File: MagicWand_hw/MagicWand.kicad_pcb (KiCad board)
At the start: 4 copper layers, 103 x 14.4 mm, 90 parts, among them M1 MOTOR_NO_CONTACTS, Q1 M28S, Q2 M28S, Q3 M28S, Q4 M28S, Q5 IRLML6401, Q6 M28S, Q7 IRLML6401, SW1 BUTTON, SW2 BUTTON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

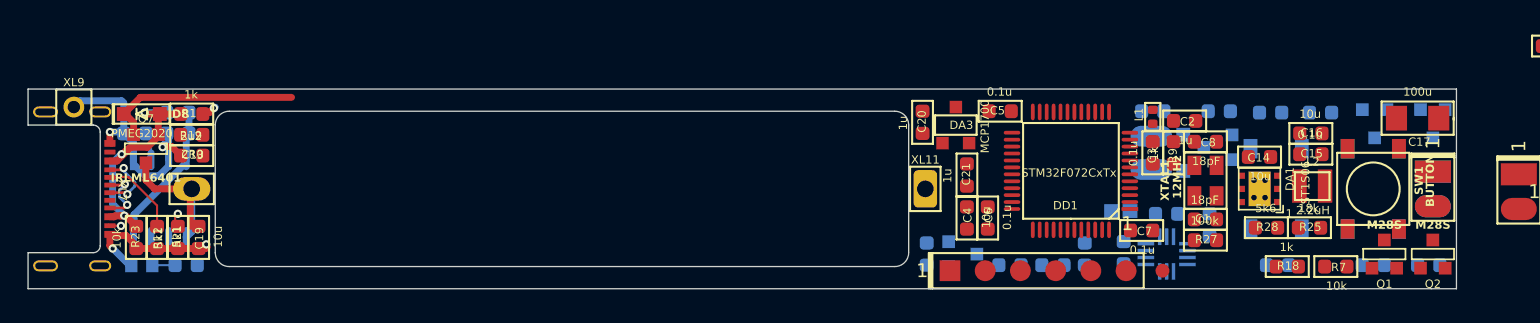
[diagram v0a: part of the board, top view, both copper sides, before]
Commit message: Remove quartz, PCB length decreased to 99mm
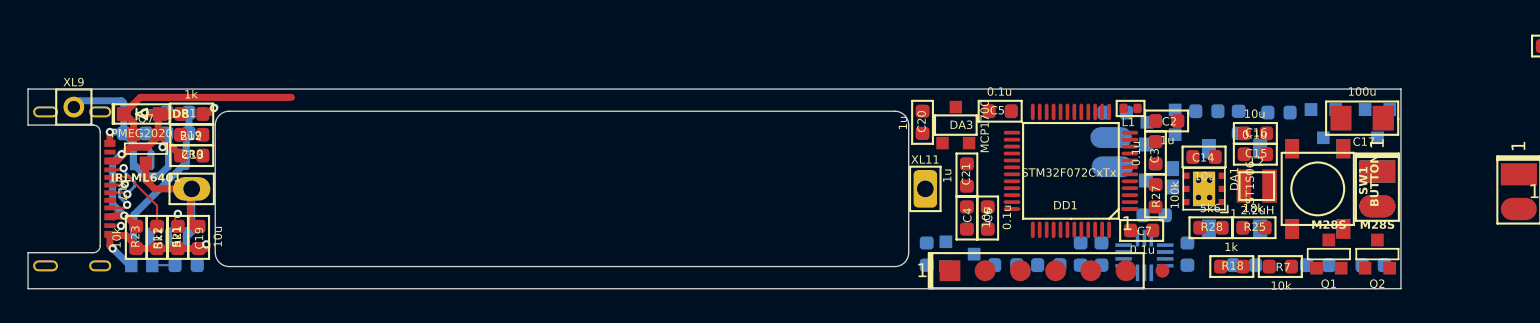
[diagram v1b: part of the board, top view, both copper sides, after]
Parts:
- removed C1, C8: 18pF, Capacitors:CAP_0603_Silks
- removed R9: 1k, Resistors:RES_0603_Silks
- removed XTAL1: 12MHz, Quartz:03225C4
- moved R27 4.82 mm to (185.3, 102.7), turned to 90 degrees
- moved Q6 4.48 mm to (185.7, 97.4)
- moved F1 4.41 mm to (186.5, 101.4), turned to -90 degrees
- moved C14 4.00 mm to (188.8, 99.9)
- moved C15 4.00 mm to (192.5, 99.7)
- moved C16 4.00 mm to (192.5, 98.2)
- moved C17 4.00 mm to (200.2, 97.1)
- moved DA1 4.00 mm to (188.8, 102.2)
- moved L2 4.00 mm to (192.6, 102.0)
- moved Q1 4.00 mm to (197.8, 106.9)
- moved Q2 4.00 mm to (201.3, 106.9)
- moved Q3 4.00 mm to (201.3, 97.5)
- moved R17 4.00 mm to (197.0, 107.7)
- moved R18 4.00 mm to (190.8, 107.8)
- moved R25 4.00 mm to (192.4, 105.0)
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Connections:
- DD1 pad 5: Net-(DD1-OSCIN) -> unconnected-(DD1-OSCIN-Pad5)
- DD1 pad 6: Net-(DD1-OSCOUT) -> unconnected-(DD1-OSCOUT-Pad6)
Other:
- board size 103 x 14.4 mm -> 99 x 14.4 mm

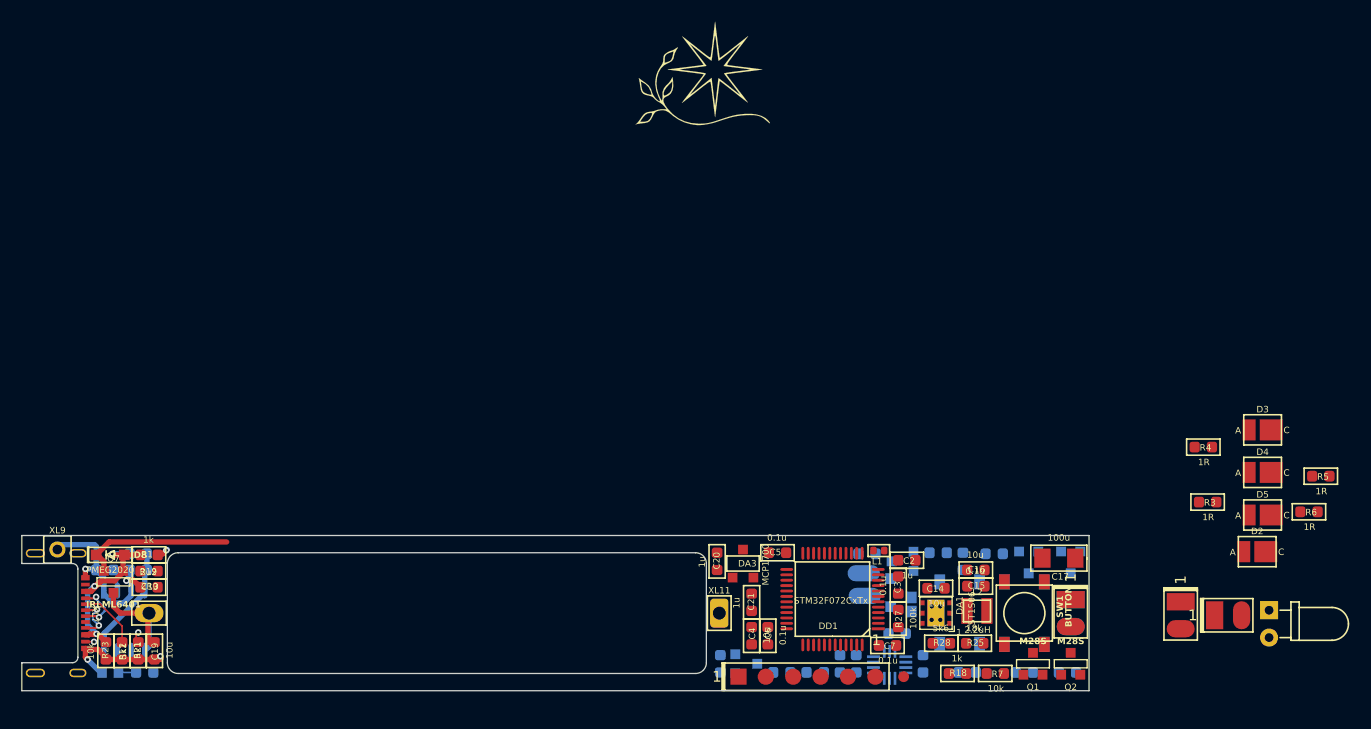
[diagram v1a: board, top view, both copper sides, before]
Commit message: USB conn changed to real one
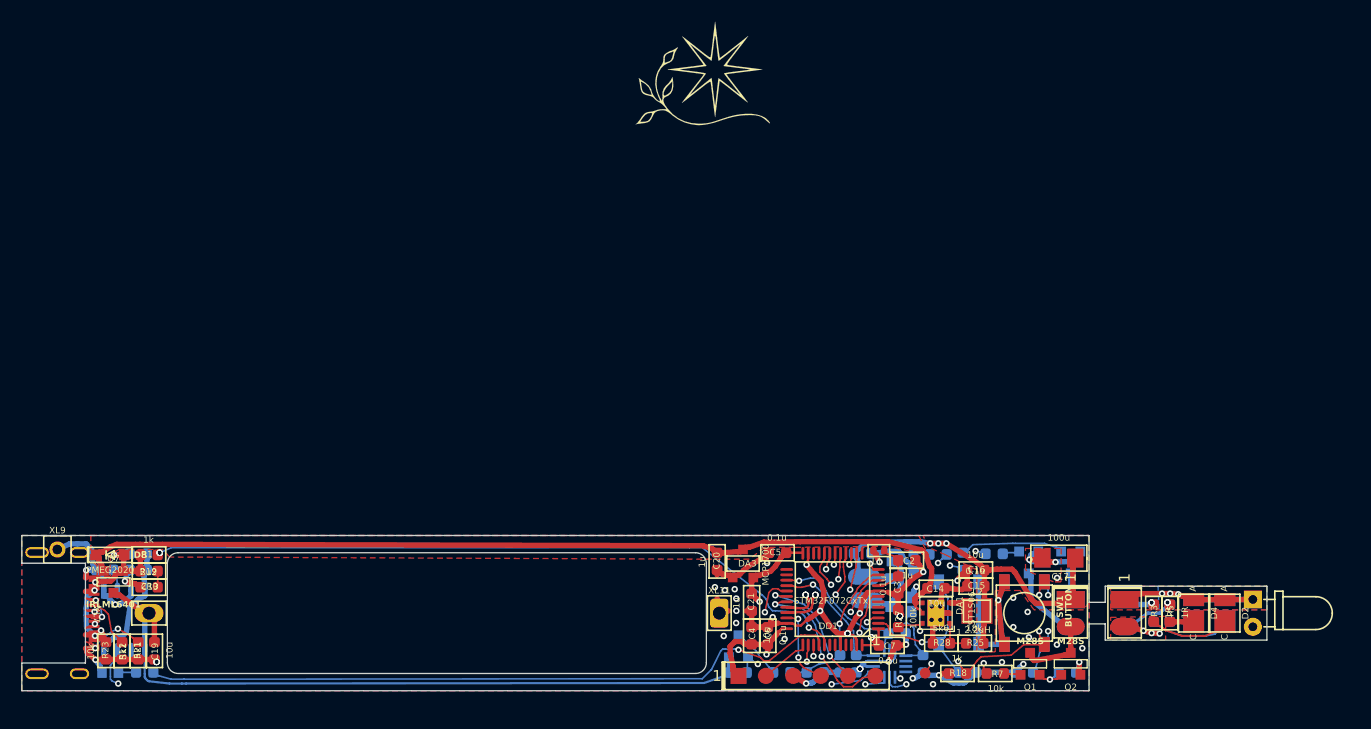
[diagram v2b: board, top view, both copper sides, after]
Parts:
- D3, D5, R4, R6, XL5: moved to B.Cu
- moved R5 18.9 mm to (210.5, 102.2), turned to 90 degrees
- moved D3 17.4 mm to (215.6, 102.2), turned to -90 degrees
- moved R4 16.1 mm to (209.0, 102.2), turned to 90 degrees
- moved R6 16.0 mm to (210.5, 102.2), turned to 90 degrees
- moved D4 14.5 mm to (212.7, 102.2), turned to -90 degrees
- moved R3 11.4 mm to (209.0, 102.2), turned to 90 degrees
- moved D5 11.1 mm to (212.7, 102.2), turned to -90 degrees
- moved XL5 9.60 mm to (206.3, 102.2), turned to -90 degrees
- moved D2 6.44 mm to (215.6, 102.2), turned to -90 degrees
- moved XL3 5.20 mm to (206.3, 102.2)
- moved TP1 2.02 mm to (187.8, 107.8)
- moved R14 1.84 mm to (170.4, 107.7), turned to 0 degrees
- moved D1 1.80 mm to (218.2, 102.2)
- moved Q5 1.78 mm to (170.5, 105.3), turned to 0 degrees
- moved XL8 0.44 mm to (182.4, 101.0)
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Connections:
- net /LED_PWR_EN renamed /PWR_EN
- net Net-(D1-PadA) renamed /LEDA
- net Net-(D1-PadC) renamed /LEDIRC
- net Net-(R3-Pad2) renamed /LEDGC
- net Net-(R5-Pad2) renamed /LEDWC
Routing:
- net GND: track 28.2 -> 260.4 mm, vias 4 -> 49
- net +PwrMCU: track 0.00 -> 83.4 mm, vias 0 -> 8
- net /USB_D+: track 4.14 -> 80.7 mm, vias 2 -> 5
- net /IS_CHARGING: track 0.00 -> 75.4 mm, vias 0 -> 2
- net /USB_D-: track 5.07 -> 80.1 mm, vias 2 -> 5
- net +PwrUnst: track 14.2 -> 88.1 mm
- net /SYS_LED: track 0.00 -> 65.2 mm, vias 0 -> 1
- net Net-(DD1-PB5): track 1.07 -> 66.2 mm, vias 1 -> 4
- net +BATT: track 11.2 -> 69.5 mm
- net +PwrCtrled: track 0.00 -> 40.6 mm, vias 0 -> 3
- net /BTN1: track 0.00 -> 31.9 mm, vias 0 -> 4
- net /BTN2: track 0.00 -> 27.0 mm, vias 0 -> 3
- net /ACC_PWR: track 0.00 -> 21.7 mm, vias 0 -> 1
- net /LEDA: track 0.00 -> 20.7 mm, vias 0 -> 3
- net /IR_LED_DAC: track 0.00 -> 18.9 mm, vias 0 -> 2
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- added copper zone on F.Cu, net +PwrCtrled
- added copper zone on F.Cu, net +PwrUnst
- added copper zone on B.Cu, net /LEDA
- added copper zone on F.Cu, net /LEDA
- added copper zone on F.Cu, net /LEDIRC
- added copper zone on In2.Cu, net /LEDIRC
- added copper zone on B.Cu, net GND
- added copper zone on F.Cu, net GND
- added copper zone on In1.Cu, net GND
- added copper zone on In2.Cu, net GND
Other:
- board size 99 x 14.4 mm -> 115.5 x 14.4 mm

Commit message: PCB sent to factory
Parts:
- Logo1: moved to B.Cu
- moved Logo1 48.4 mm to (174.5, 100.0), turned to 180 degrees
- moved XL1 13.0 mm to (183.4, 107.9), turned to 180 degrees
- moved R12 1.80 mm to (115.1, 105.8)
- moved R21 1.20 mm to (113.6, 105.8)
- moved Q7 0.41 mm to (112.9, 99.2)
- moved C19 0.32 mm to (116.6, 105.8)
- moved R23 0.32 mm to (112.1, 105.8)
- moved XL9 0.26 mm to (107.5, 96.1)
- moved D8 0.10 mm to (112.3, 96.8)
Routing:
- net +5vUSB: track 22.8 -> 36.5 mm, vias 5 -> 3
- net /USB_D+: track 80.7 -> 88.4 mm, vias 5 -> 3
- net /USB_D-: track 80.1 -> 87.7 mm, vias 5 -> 3
- net GND: track 260.4 -> 253.1 mm, vias 49 -> 47
- net /UART_TX: track 11.8 -> 16.6 mm, vias 2 -> 0
- net /UART_RX: track 15.4 -> 11.0 mm, vias 2 -> 0
- net /USB_CC2_IN: track 6.28 -> 3.56 mm, vias 2 -> 0
- net +PwrUnst: track 88.1 -> 85.6 mm
- net +PwrMCU: track 83.4 -> 81.5 mm, vias 8 -> 6
- net /SWCLK: track 4.73 -> 6.12 mm
- net /USB_CC1_IN: track 5.44 -> 6.71 mm
- net /ACC_MISO: track 17.0 -> 16.0 mm
- net Net-(DD1-PB5): track 66.2 -> 65.3 mm, vias 4 -> 2
- net /BAT_MEAS_EN: track 11.1 -> 10.3 mm
- net /ACC_CS: track 11.3 -> 10.6 mm
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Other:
- rule pad_to_mask_clearance: 0 -> 0.06
- board text added: "+"
- board text added: "A"
- board text added: "G"
- board text added: "GND"
- board text added: "IRC"
- board text added: "Ostranna Magic Wand v1"
- board text added: "W"
